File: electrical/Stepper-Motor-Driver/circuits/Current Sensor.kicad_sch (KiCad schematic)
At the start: 6 parts, among them U2 INA240A2PW, U5 ADS7042xDCU

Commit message: Symbol cleanup and initial power section design
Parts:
- C1, C2, C3: footprint (none) -> Capacitor_SMD:C_1206_3216Metric
- R_Shunt1: footprint LVK25R010DE:LVK25R010DE -> Resistor_SMD:R_Shunt_Ohmite_LVK25
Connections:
- net +3.3V: now also C3.1; no longer C2.2, C3.2, U2.6 (REF2), U5.7 (AVDD)
- net GND: now also C2.2, C3.2; no longer C2.1, C3.1, U2.7 (REF1)
- new net +1.65V-REF: U2.6 (REF2), U2.7 (REF1)
- new net +3.3V-REF: C2.1, U5.7 (AVDD)
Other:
- moved on the sheet: C2, C3

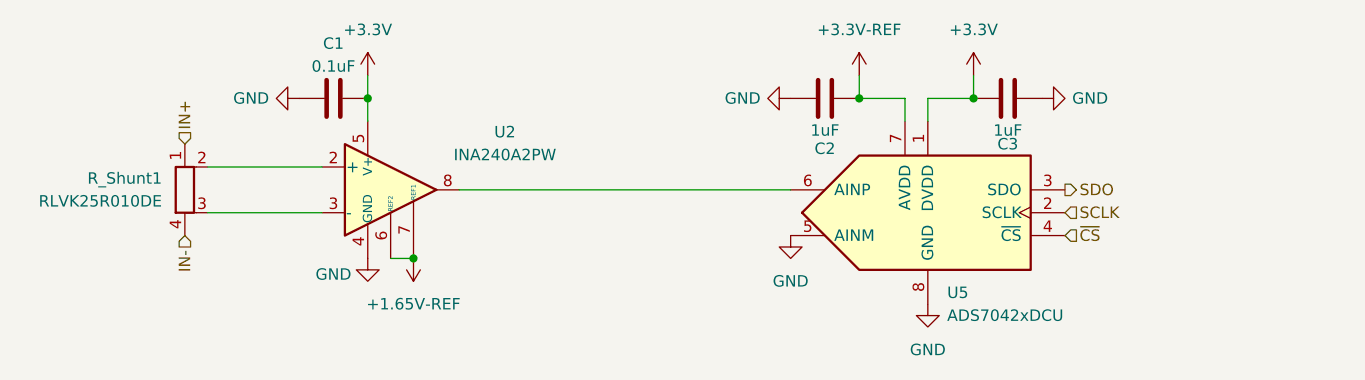
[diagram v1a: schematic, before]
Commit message: Adding test points and FPGA sockets
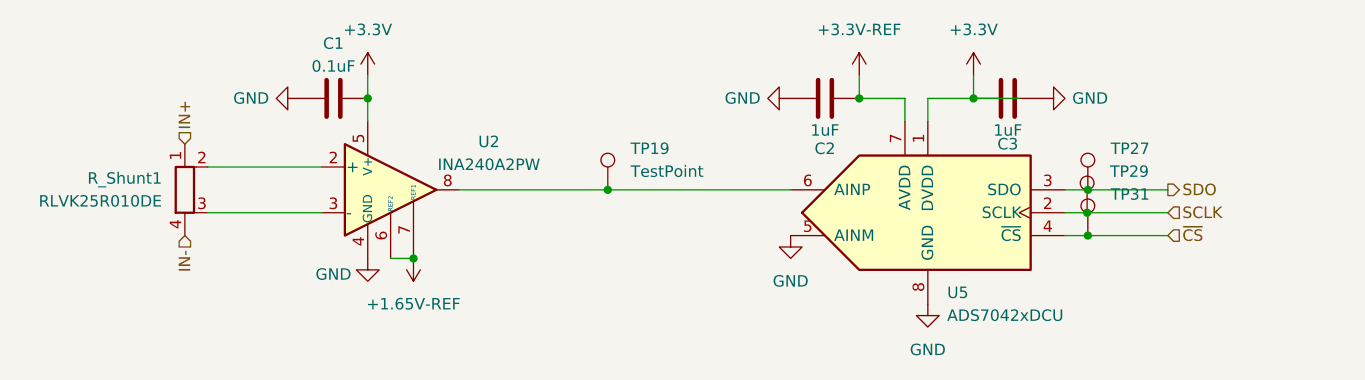
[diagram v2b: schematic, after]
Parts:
- added TP19, TP27, TP29, TP31: TestPoint, Connector_PinHeader_1.00mm:PinHeader_1x01_P1.00mm_Vertical, symbol Connector:TestPoint
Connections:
- net SCLK: now also TP29.1
- net SDO: now also TP27.1
- net ~{CS}: now also TP31.1
- net at U2.8, U5.6 (AINP): now also TP19.1

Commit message: Initial PCB layout
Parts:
- R_Shunt1: value RLVK25R010DE -> LVK12R010CER; footprint Resistor_SMD:R_Shunt_Ohmite_LVK25 -> Resistor_SMD:R_Shunt_Ohmite_LVK12
- renumbered C1 to C17, C2 to C18, C3 to C19, TP19 to TP17, TP27 to TP18, TP31 to TP19, TP29 to TP20, U2 to U6, U5 to U7
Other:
- moved on the sheet: TP19, TP20

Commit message: Ensuring continuous ground plane below analog section
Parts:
- removed TP18: TestPoint, Connector_PinHeader_1.00mm:PinHeader_1x01_P1.00mm_Vertical, symbol Connector:TestPoint
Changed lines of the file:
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@@
 		(color 0 0 0 0)
 	)
-	(junction
-		(at 207.01 58.42)
-		(diameter 0)
-		(color 0 0 0 0)
-	)
 	(wire
 		(pts
@@
 	(wire
 		(pts
-			(xy 207.01 58.42) (xy 215.9 58.42)
-		)
-		(stroke
-			(width 0)
-			(type default)
-		)
-	)
-	(wire
-		(pts
 			(xy 204.47 60.96) (xy 224.79 60.96)
 		)
@@
 	(wire
 		(pts
-			(xy 204.47 58.42) (xy 207.01 58.42)
+			(xy 204.47 58.42) (xy 215.9 58.42)
 		)
 		(stroke
@@
 					(unit 1)
 				)
-			)
-		)
-	)
-	(symbol
-		(lib_id "Connector:TestPoint")
-		(at 207.01 58.42 0)
-		(unit 1)
-		(body_style 1)
-		(exclude_from_sim no)
-		(in_bom yes)
-		(on_board yes)
-		(in_pos_files yes)
-		(dnp no)
-		(fields_autoplaced yes)
-		(property "Reference" "TP18"
-			(at 209.55 53.8479 0)
-			(show_name no)
-			(do_not_autoplace no)
-			(effects
-				(font
-					(size 1.27 1.27)
-				)
-				(justify left)
-			)
-		)
-		(property "Value" "TestPoint"
-			(at 209.55 56.3879 0)
-			(hide yes)
-			(show_name no)
-			(do_not_autoplace no)
-			(effects
-				(font
-					(size 1.27 1.27)
-				)
-				(justify left)
-			)
-		)
-		(property "Footprint" "Connector_PinHeader_1.00mm:PinHeader_1x01_P1.00mm_Vertical"
-			(at 212.09 58.42 0)
-			(hide yes)
-			(show_name no)
-			(do_not_autoplace no)
-			(effects
-				(font
-					(size 1.27 1.27)
-				)
-			)
-		)
-		(property "Datasheet" ""
-			(at 212.09 58.42 0)
-			(hide yes)
-			(show_name no)
-			(do_not_autoplace no)
-			(effects
-				(font
-					(size 1.27 1.27)
-				)
-			)
-		)
-		(property "Description" "test point"
-			(at 207.01 58.42 0)
-			(hide yes)
-			(show_name no)
-			(do_not_autoplace no)
-			(effects
-				(font
-					(size 1.27 1.27)
-				)
-			)
-		)
-		(pin "1"
-		)
-		(instances
-			(project "Stepper Motor Driver"
-				(path "/c25060f1-f2f3-4cbd-b6ee-5f66e19502f5/06fa326d-3253-4b51-93b8-81e3e564f7d6"
-					(reference "TP18")
-					(unit 1)
-				)
-				(path "/c25060f1-f2f3-4cbd-b6ee-5f66e19502f5/dc8574df-72f0-4dd6-9c05-ed1f6574d07d"
-					(reference "TP22")
-					(unit 1)
-				)
